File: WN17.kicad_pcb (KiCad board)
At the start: 2 copper layers, 41 x 46 mm, 14 parts, among them J1 Conn_01x02_Pin, U1 AS5600, U2 DRV8434APWPR, U3 STM32L476RGTx, U4 ESP-12F, U5 AMS1117

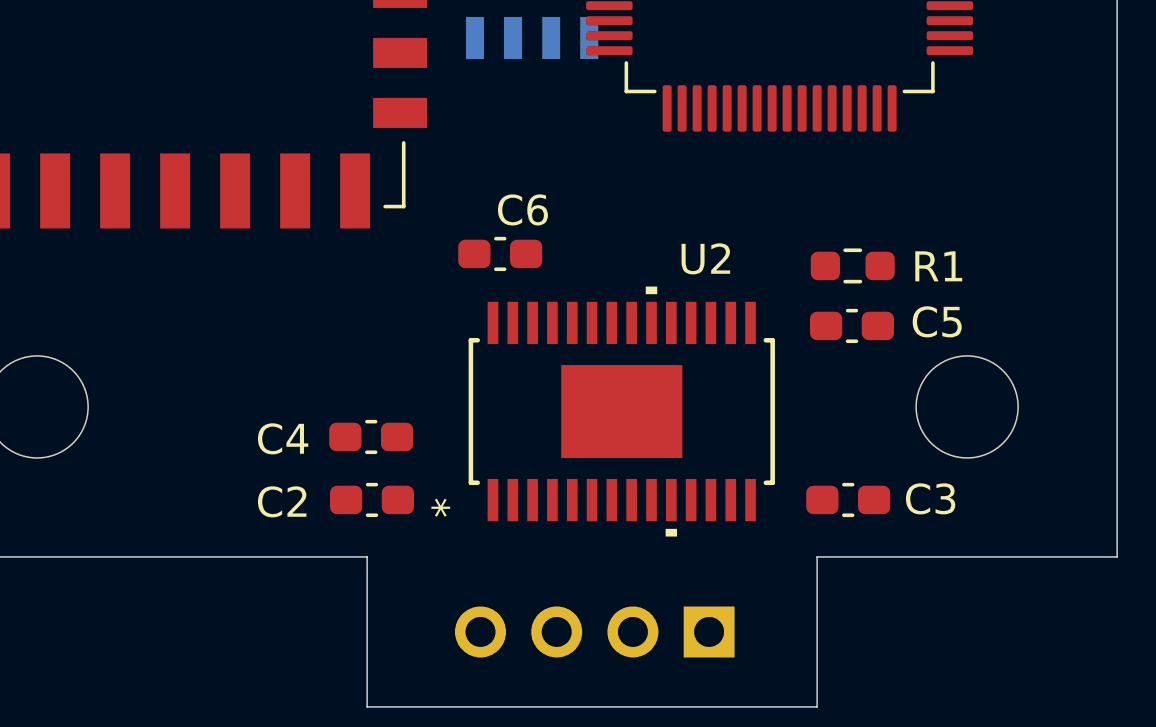
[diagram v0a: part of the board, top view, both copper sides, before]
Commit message: Moved driver to better position
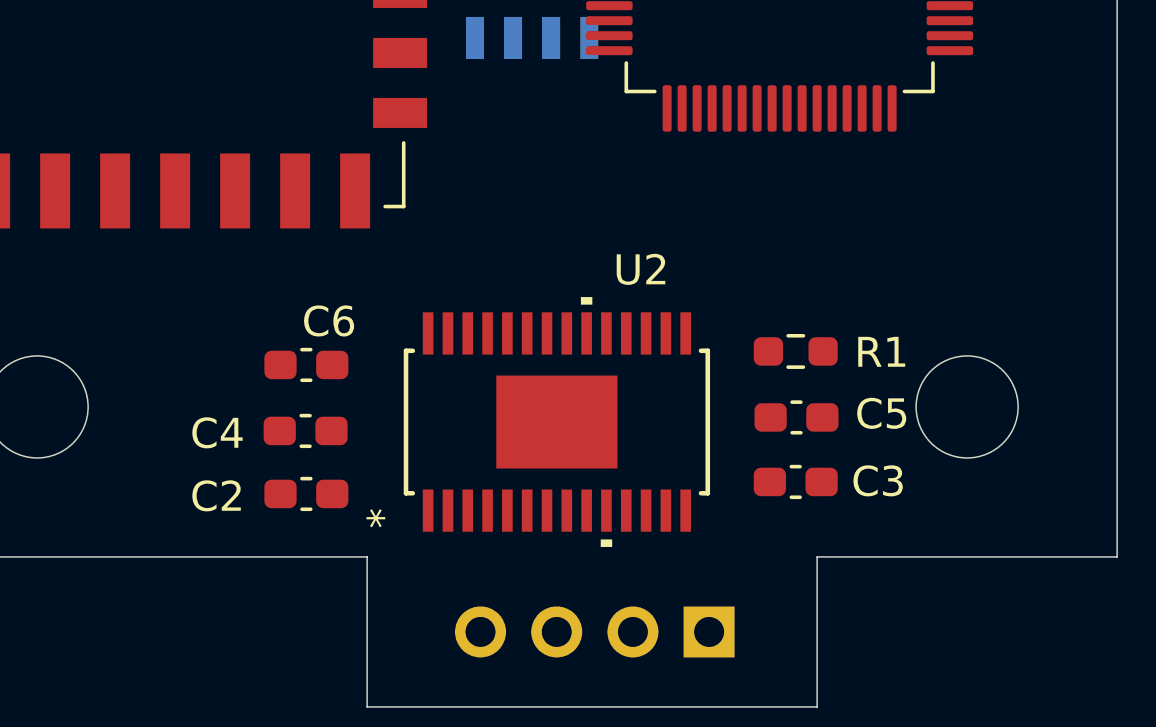
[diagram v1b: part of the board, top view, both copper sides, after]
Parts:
- moved C6 7.45 mm to (109.0, 89.6)
- moved C5 3.57 mm to (125.3, 91.3)
- moved R1 3.43 mm to (125.3, 89.2)
- moved C4 2.20 mm to (109.0, 91.8)
- moved C2 2.20 mm to (109.0, 93.9)
- moved U2 2.19 mm to (117.3, 91.5)
- moved C3 1.85 mm to (125.3, 93.5)
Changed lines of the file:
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@@
 	(footprint "Capacitor_SMD:C_0603_1608Metric_Pad1.08x0.95mm_HandSolder"
 		(layer "F.Cu")
-		(at 115.4375 85.9)
+		(at 108.975 89.6)
 		(descr "Capacitor SMD 0603 (1608 Metric), square (rectangular) end terminal, IPC_7351 nominal with elongated pad for handsoldering. (Body size source: IPC-SM-782 page 76, https://www.pcb-3d.com/wordpress/wp-content/uploads/ipc-sm-782a_amendment_1_and_2.pdf), generated with kicad-footprint-generator")
 		(tags "capacitor handsolder")
@@
 	(footprint "Capacitor_SMD:C_0603_1608Metric_Pad1.08x0.95mm_HandSolder"
 		(layer "F.Cu")
-		(at 111.1375 92)
+		(at 108.95 91.8)
 		(descr "Capacitor SMD 0603 (1608 Metric), square (rectangular) end terminal, IPC_7351 nominal with elongated pad for handsoldering. (Body size source: IPC-SM-782 page 76, https://www.pcb-3d.com/wordpress/wp-content/uploads/ipc-sm-782a_amendment_1_and_2.pdf), generated with kicad-footprint-generator")
 		(tags "capacitor handsolder")
@@
 	(footprint "Capacitor_SMD:C_0603_1608Metric_Pad1.08x0.95mm_HandSolder"
 		(layer "F.Cu")
-		(at 127.0375 94.1)
+		(at 125.2875 93.5)
 		(descr "Capacitor SMD 0603 (1608 Metric), square (rectangular) end terminal, IPC_7351 nominal with elongated pad for handsoldering. (Body size source: IPC-SM-782 page 76, https://www.pcb-3d.com/wordpress/wp-content/uploads/ipc-sm-782a_amendment_1_and_2.pdf), generated with kicad-footprint-generator")
 		(tags "capacitor handsolder")
@@
 	(footprint "Capacitor_SMD:C_0603_1608Metric_Pad1.08x0.95mm_HandSolder"
 		(layer "F.Cu")
-		(at 127.1625 88.3)
+		(at 125.3125 91.35)
 		(descr "Capacitor SMD 0603 (1608 Metric), square (rectangular) end terminal, IPC_7351 nominal with elongated pad for handsoldering. (Body size source: IPC-SM-782 page 76, https://www.pcb-3d.com/wordpress/wp-content/uploads/ipc-sm-782a_amendment_1_and_2.pdf), generated with kicad-footprint-generator")
 		(tags "capacitor handsolder")
@@
 	(footprint "Capacitor_SMD:C_0603_1608Metric_Pad1.08x0.95mm_HandSolder"
 		(layer "F.Cu")
-		(at 111.1625 94.1 180)
+		(at 108.975 93.9 180)
 		(descr "Capacitor SMD 0603 (1608 Metric), square (rectangular) end terminal, IPC_7351 nominal with elongated pad for handsoldering. (Body size source: IPC-SM-782 page 76, https://www.pcb-3d.com/wordpress/wp-content/uploads/ipc-sm-782a_amendment_1_and_2.pdf), generated with kicad-footprint-generator")
 		(tags "capacitor handsolder")
@@
 	(footprint "Resistor_SMD:R_0603_1608Metric_Pad0.98x0.95mm_HandSolder"
 		(layer "F.Cu")
-		(at 127.1875 86.3)
+		(at 125.2875 89.15)
 		(descr "Resistor SMD 0603 (1608 Metric), square (rectangular) end terminal, IPC_7351 nominal with elongated pad for handsoldering. (Body size source: IPC-SM-782 page 72, https://www.pcb-3d.com/wordpress/wp-content/uploads/ipc-sm-782a_amendment_1_and_2.pdf), generated with kicad-footprint-generator")
 		(tags "resistor handsolder")
@@
 	(footprint "drv8411:DRV8434APWPR_TEX"
 		(layer "F.Cu")
-		(at 119.4886 91.15275 90)
+		(at 117.3261 91.50275 90)
 		(tags "DRV8434APWPR ")
 		(property "Reference" "U2"
